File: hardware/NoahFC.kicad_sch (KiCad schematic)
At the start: 44 parts, among them J1 ALE, J11 SCK, J12 MISO, J17 VTX, J18 RESET, J2 ELE, J3 CAM, J4 FTDI, J5 VCC, J6 THR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

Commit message: rev4 project
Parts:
- removed C20: 4.7uF, Capacitor_SMD:C_0805_2012Metric, symbol Device:C
- removed C21: 220nF, Capacitor_SMD:C_0805_2012Metric, symbol Device:C
- removed D3: PWR, LED_SMD:LED_0805_2012Metric, symbol Device:LED
- removed J11: SCK, TestPoint:TestPoint_Pad_1.0x1.0mm, symbol Connector:Conn_01x01_Female
- removed J12: MISO, TestPoint:TestPoint_Pad_1.0x1.0mm, symbol Connector:Conn_01x01_Female
- removed J17: VTX, Connector_PinHeader_2.54mm:PinHeader_1x03_P2.54mm_Vertical, symbol Connector:Conn_01x03_Male
- removed J18: RESET, TestPoint:TestPoint_Pad_1.0x1.0mm, symbol Connector:Conn_01x01_Female
- removed J3: CAM, Connector_PinHeader_2.54mm:PinHeader_1x03_P2.54mm_Vertical, symbol Connector:Conn_01x03_Male
- removed R4: 330, Resistor_SMD:R_0805_2012Metric, symbol Device:R
- removed U6: HMC5883L, LPCC-16, symbol HMC5883L:HMC5883L
- removed Y2: 27Mhz, Crystal:Crystal_SMD_3225-4Pin_3.2x2.5mm, symbol Device:Resonator
- added C1, C2, C4: 100nF, Capacitor_SMD:C_0805_2012Metric, symbol Device:C
- added J13: OSD, Connector_JST:JST_SH_BM05B-SRSS-TB_1x05-1MP_P1.00mm_Vertical, symbol Connector:Conn_01x05_Socket
- added Y3: 27Mhz, Crystal:Crystal_SMD_3225-4Pin_3.2x2.5mm, symbol Device:Crystal_GND24
- C11: value 22uF -> 10uF
- J1, J2, J6, J7: symbol Connector:Conn_01x03_Female -> Connector:Conn_01x03_Socket
- J4: footprint Connector_PinHeader_2.54mm:PinHeader_1x05_P2.54mm_Vertical -> Connector_JST:JST_SH_BM05B-SRSS-TB_1x05-1MP_P1.00mm_Vertical; symbol Connector:Conn_01x05_Female -> Connector:Conn_01x05_Socket
- J5: symbol Connector:Conn_01x01_Female -> Connector:Conn_01x01_Socket
- J8: footprint Connector_PinHeader_2.54mm:PinHeader_1x04_P2.54mm_Vertical -> Connector_JST:JST_SH_BM04B-SRSS-TB_1x04-1MP_P1.00mm_Vertical; symbol Connector:Conn_01x04_Female -> Connector:Conn_01x04_Socket
- R7, R8: value 10K -> 4.7K
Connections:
- net 3.3V: now also C6.1, C7.2; no longer C6.2, C7.1
- net 5V: now also U5.19 (~{RESET}), C1.1, C2.1, C4.1, J13.5 (Pin_5)
- net GND: now also C6.2, C7.1, C1.2, C2.2, C4.2, J13.2 (Pin_2), J13.4 (Pin_4); no longer C6.1, C7.2
- net SCL: now also R8.2; no longer R7.2
- net SDA: now also R7.2; no longer R8.2
- net XTAL1_OSD: now also U5.5 (CLKIN), Y3.1; no longer U5.6 (XFB)
- net XTAL2_OSD: now also U5.6 (XFB), Y3.3; no longer U5.5 (CLKIN)
- net at C17.2, R9.1: now also J13.1 (Pin_1)
- net SAG: now reaches C19.1
- net SAG: now also U5.25 (SAG); no longer U5.26 (VOUT)
- net VIN: now reaches C17.1, U5.22 (VIN)
- net at R10.2: now also J13.3 (Pin_3)
- net VOUT: now reaches C18.1
- net VOUT: now also U5.26 (VOUT); no longer U5.25 (SAG)
- no-connect marks 23 -> 16
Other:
- moved on the sheet: U1, U2, U4, U5

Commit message: add bottom labels
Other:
- title: (none) -> NoahFC
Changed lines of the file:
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@@
 (kicad_sch (version 20230121) (generator eeschema)
   (paper "A4")
+  (title_block
+    (title "NoahFC")
+    (rev "4")
+  )
   (junction (at 238.76 64.77) (diameter 0) (color 0 0 0 0)
   )

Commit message: update project rev5
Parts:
- removed J5: VCC, TestPoint:TestPoint_Pad_1.5x1.5mm, symbol Connector:Conn_01x01_Socket
- removed R5: 100K, Resistor_SMD:R_0805_2012Metric, symbol Device:R
- removed R6: 10K, Resistor_SMD:R_0805_2012Metric, symbol Device:R
- removed U4: AMS1117-3.3, Package_TO_SOT_SMD:SOT-223-3_TabPin2, symbol Regulator_Linear:AP1117-33
- added U3: XC6206PxxxMR, Package_TO_SOT_SMD:SOT-23-3, symbol Regulator_Linear:XC6206PxxxMR
- C10, C11: value 10uF -> 1uF
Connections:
- net 3.3V: now also U3.2 (VO)
- net 5V: now also U3.3 (VI)
- net GND: now also U3.1 (GND)
- net VOLTAGE_READ: no longer names the net of U1.23 (PC0)
- no-connect marks 16 -> 17

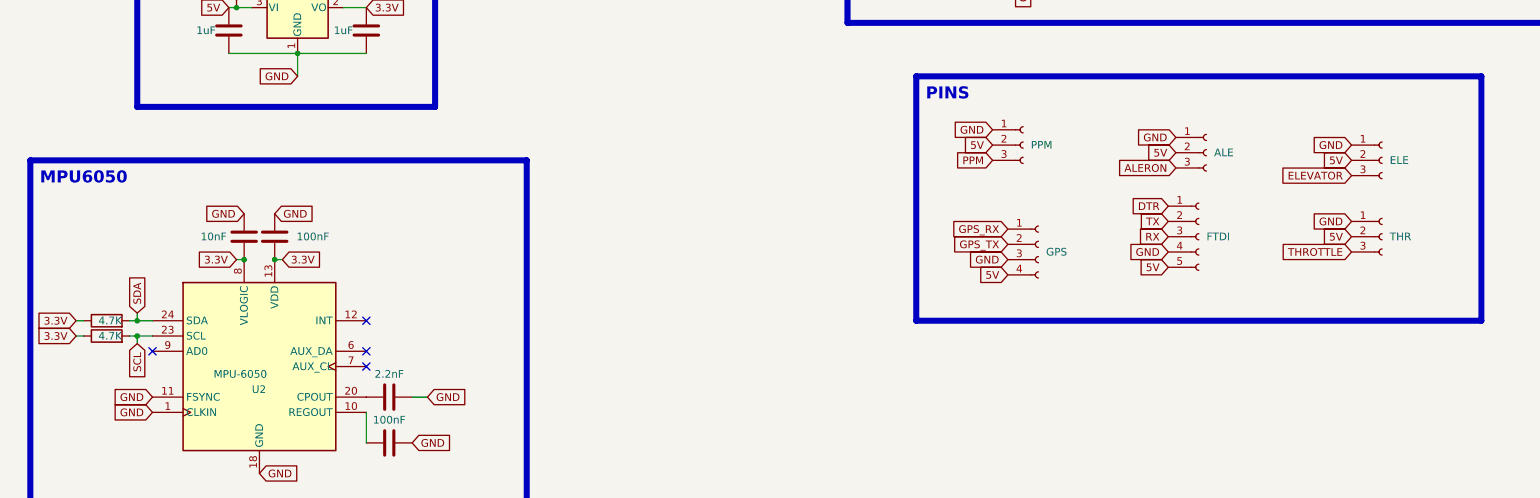
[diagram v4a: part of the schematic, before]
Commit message: add sda scl pinout
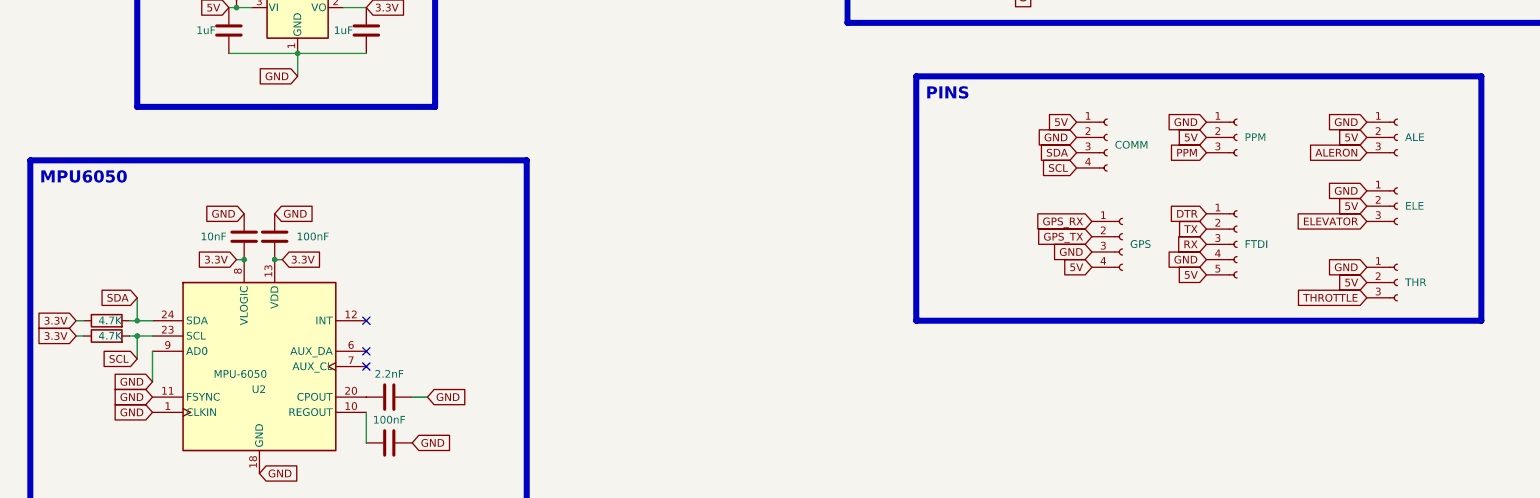
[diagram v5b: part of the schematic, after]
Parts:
- added J3: COMM, Connector_JST:JST_SH_BM04B-SRSS-TB_1x04-1MP_P1.00mm_Vertical, symbol Connector:Conn_01x04_Socket
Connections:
- net 5V: now also J3.1 (Pin_1)
- net GND: now also U2.9 (AD0), J3.2 (Pin_2)
- net SCL: now also J3.4 (Pin_4)
- net SDA: now also J3.3 (Pin_3)
- no-connect marks 17 -> 16

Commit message: add jumper, organize pcb
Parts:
- added JP1: power from servo, Jumper:SolderJumper-2_P1.3mm_Open_RoundedPad1.0x1.5mm, symbol Jumper:SolderJumper_2_Open
- U3: value XC6206PxxxMR -> XC6206P332MR
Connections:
- net 5V: now also JP1.1 (A); no longer J1.2 (Pin_2), J2.2 (Pin_2), J6.2 (Pin_2), J7.2 (Pin_2)
- new net 5V-BEC: J1.2 (Pin_2), J2.2 (Pin_2), J6.2 (Pin_2), J7.2 (Pin_2), JP1.2 (B)
